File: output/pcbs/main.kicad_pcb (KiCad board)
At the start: 2 copper layers, 125.8 x 86.6 mm, 22 parts

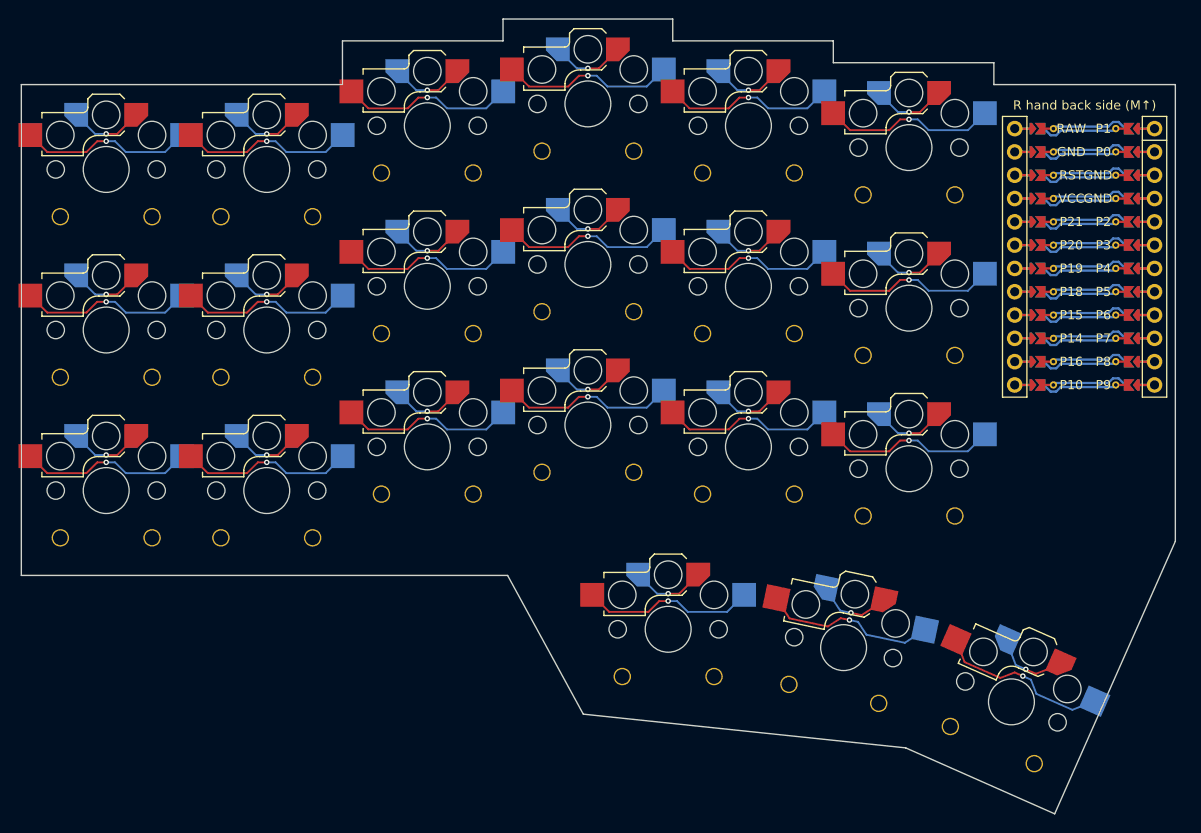
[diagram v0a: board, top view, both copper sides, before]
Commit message: feat: add more ref pos (9-14) and ref corners
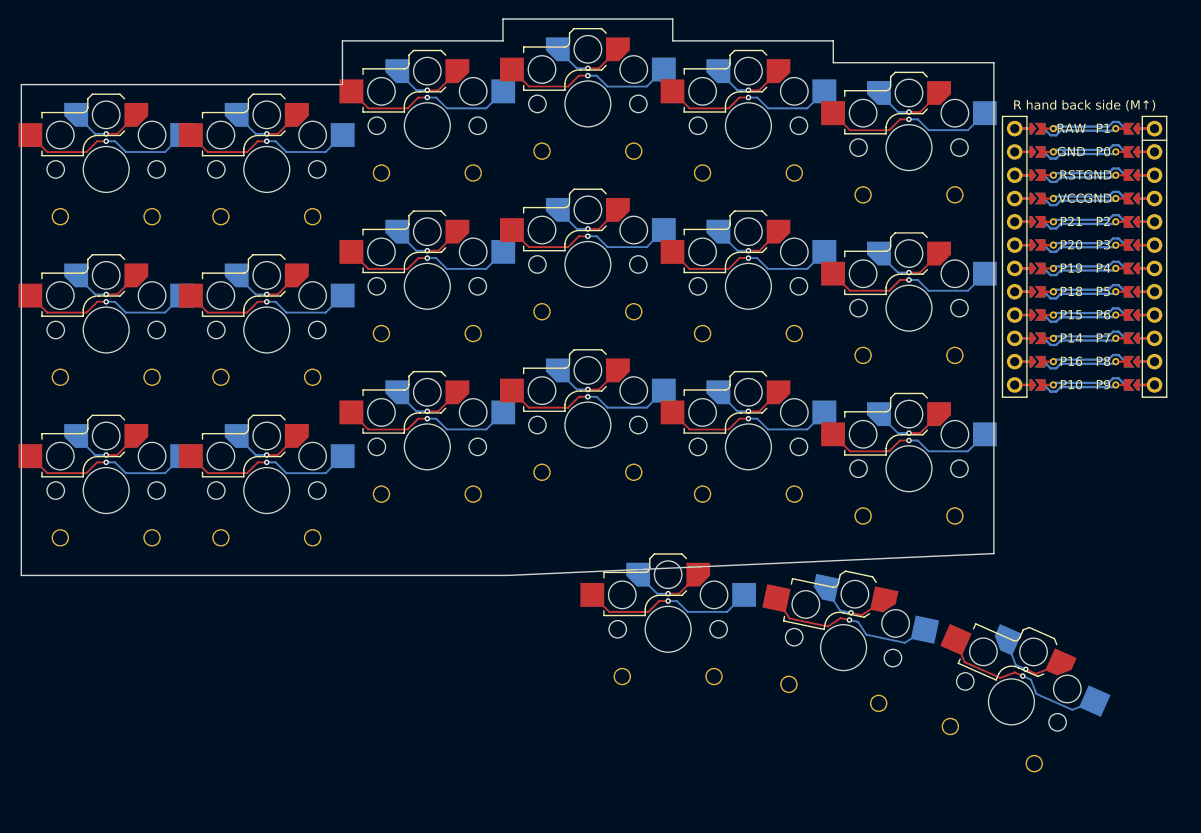
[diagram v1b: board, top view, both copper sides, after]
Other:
- board size 125.8 x 86.6 mm -> 106 x 60.6 mm

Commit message: refactor: minor refactor
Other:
- board size 106 x 60.6 mm -> 120.1 x 86.6 mm
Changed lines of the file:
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@@
   (title_block
     (title "main")
-    (date "2025-01-11")
+    (date "2025-01-12")
     (rev "v1.0.0")
     (company "Unknown")
@@
   (segment (start 110.340305 -12.235) (end 109.739695 -12.235) (width 0.25) (layer "B.Cu"))
   (segment (start 109.739695 -12.235) (end 109.234695 -11.73) (width 0.25) (layer "B.Cu"))
-  (gr_line (start 96.75 6.869) (end 96.75 -46.631) (layer Edge.Cuts) (stroke (width 0.15) (type default)))
-(gr_line (start -9.25 9.25) (end 43.75 9.25) (layer Edge.Cuts) (stroke (width 0.15) (type default)))
-(gr_line (start 25.75 -44.25) (end -9.25 -44.25) (layer Edge.Cuts) (stroke (width 0.15) (type default)))
-(gr_line (start -9.25 -44.25) (end -9.25 9.25) (layer Edge.Cuts) (stroke (width 0.15) (type default)))
+  (gr_line (start -9.25 9.25) (end 43.75 9.25) (layer Edge.Cuts) (stroke (width 0.15) (type default)))
+(gr_line (start -9.25 9.25) (end -9.25 -44.25) (layer Edge.Cuts) (stroke (width 0.15) (type default)))
+(gr_line (start -9.25 -44.25) (end 25.75 -44.25) (layer Edge.Cuts) (stroke (width 0.15) (type default)))
+(gr_line (start 25.75 -44.25) (end 25.75 -49.012) (layer Edge.Cuts) (stroke (width 0.15) (type default)))
 (gr_line (start 25.75 -49.012) (end 43.25 -49.012) (layer Edge.Cuts) (stroke (width 0.15) (type default)))
-(gr_line (start 25.75 -49.012) (end 25.75 -44.25) (layer Edge.Cuts) (stroke (width 0.15) (type default)))
-(gr_line (start 61.75 -49.012) (end 61.75 -51.393) (layer Edge.Cuts) (stroke (width 0.15) (type default)))
-(gr_line (start 61.75 -51.393) (end 43.25 -51.393) (layer Edge.Cuts) (stroke (width 0.15) (type default)))
-(gr_line (start 43.25 -51.393) (end 43.25 -49.012) (layer Edge.Cuts) (stroke (width 0.15) (type default)))
-(gr_line (start 79.25 -46.631) (end 79.25 -49.012) (layer Edge.Cuts) (stroke (width 0.15) (type default)))
+(gr_line (start 43.25 -49.012) (end 43.25 -51.393) (layer Edge.Cuts) (stroke (width 0.15) (type default)))
+(gr_line (start 43.25 -51.393) (end 61.75 -51.393) (layer Edge.Cuts) (stroke (width 0.15) (type default)))
+(gr_line (start 61.75 -51.393) (end 61.75 -49.012) (layer Edge.Cuts) (stroke (width 0.15) (type default)))
 (gr_line (start 61.75 -49.012) (end 79.25 -49.012) (layer Edge.Cuts) (stroke (width 0.15) (type default)))
+(gr_line (start 79.25 -49.012) (end 79.25 -46.631) (layer Edge.Cuts) (stroke (width 0.15) (type default)))
 (gr_line (start 79.25 -46.631) (end 96.75 -46.631) (layer Edge.Cuts) (stroke (width 0.15) (type default)))
-(gr_line (start 96.75 6.869) (end 43.75 9.25) (layer Edge.Cuts) (stroke (width 0.15) (type default)))
+(gr_line (start 96.75 -46.631) (end 96.75 6.869) (layer Edge.Cuts) (stroke (width 0.15) (type default)))
+(gr_line (start 43.75 9.25) (end 52 24.369) (layer Edge.Cuts) (stroke (width 0.15) (type default)))
+(gr_line (start 52 24.369) (end 87.1375839 28.0435087) (layer Edge.Cuts) (stroke (width 0.15) (type default)))
+(gr_line (start 87.1375839 28.0435087) (end 103.3780884 35.2335285) (layer Edge.Cuts) (stroke (width 0.15) (type default)))
+(gr_line (start 103.3780884 35.2335285) (end 110.8673033 18.317215) (layer Edge.Cuts) (stroke (width 0.15) (type default)))
+(gr_line (start 110.8673033 18.317215) (end 93.9509898 10.8280001) (layer Edge.Cuts) (stroke (width 0.15) (type default)))
+(gr_line (start 93.9509898 10.8280001) (end 96.75 6.869) (layer Edge.Cuts) (stroke (width 0.15) (type default)))
 )

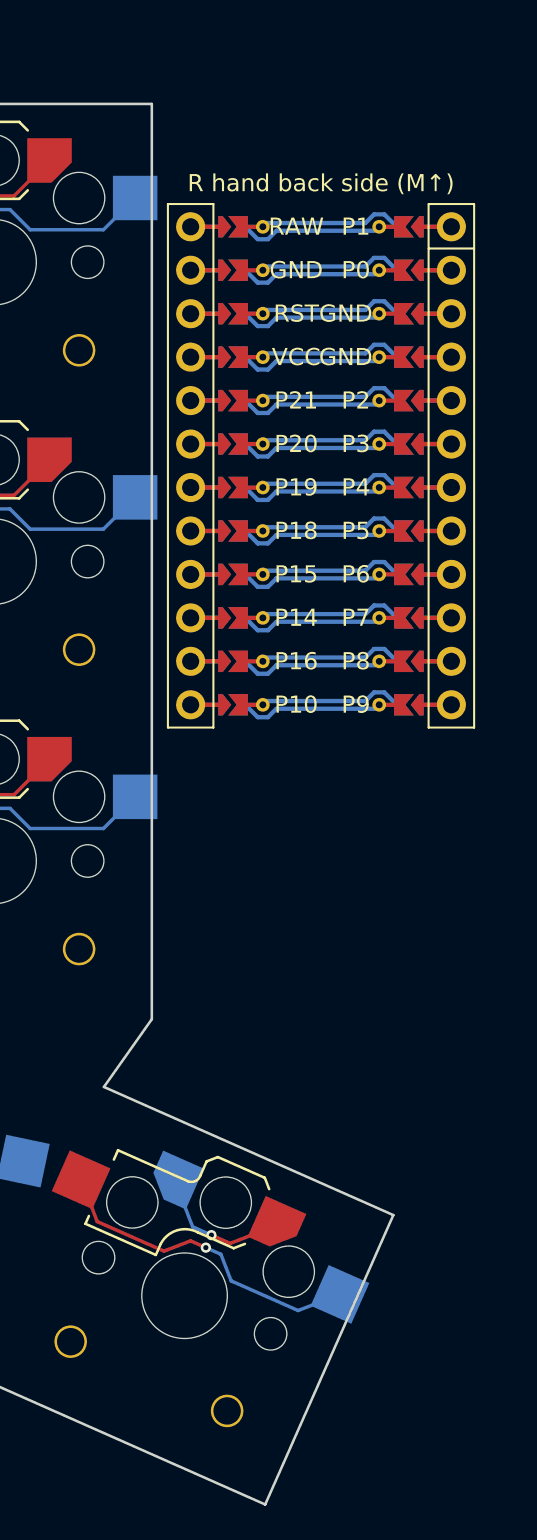
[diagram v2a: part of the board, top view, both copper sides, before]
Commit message: feat: update mcu plate calculations
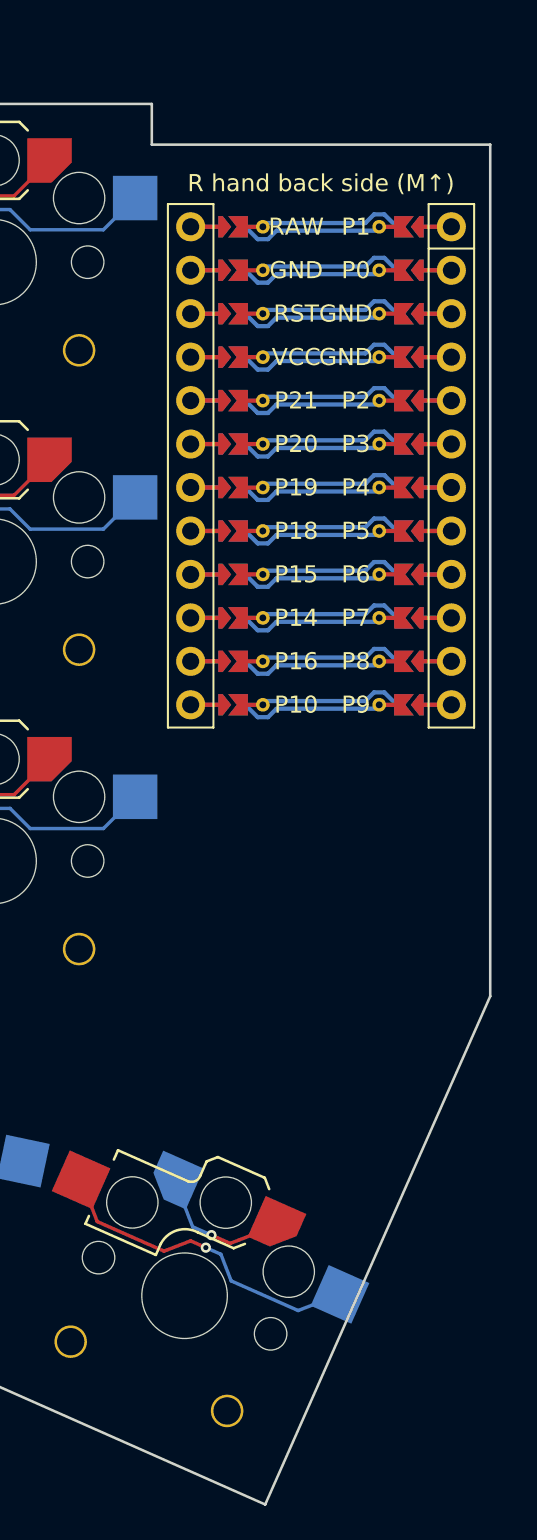
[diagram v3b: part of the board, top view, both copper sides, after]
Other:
- board size 120.1 x 86.6 mm -> 125.8 x 86.6 mm
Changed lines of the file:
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@@
   (segment (start 110.340305 -12.235) (end 109.739695 -12.235) (width 0.25) (layer "B.Cu"))
   (segment (start 109.739695 -12.235) (end 109.234695 -11.73) (width 0.25) (layer "B.Cu"))
-  (gr_line (start -9.25 9.25) (end 43.75 9.25) (layer Edge.Cuts) (stroke (width 0.15) (type default)))
+  (gr_line (start 96.75 -44.25) (end 116.53 -44.25) (layer Edge.Cuts) (stroke (width 0.15) (type default)))
+(gr_line (start 116.53 -44.25) (end 116.53 5.5265615) (layer Edge.Cuts) (stroke (width 0.15) (type default)))
+(gr_line (start 103.3780884 35.2335285) (end 116.53 5.5265615) (layer Edge.Cuts) (stroke (width 0.15) (type default)))
+(gr_line (start -9.25 9.25) (end 43.75 9.25) (layer Edge.Cuts) (stroke (width 0.15) (type default)))
 (gr_line (start -9.25 9.25) (end -9.25 -44.25) (layer Edge.Cuts) (stroke (width 0.15) (type default)))
 (gr_line (start -9.25 -44.25) (end 25.75 -44.25) (layer Edge.Cuts) (stroke (width 0.15) (type default)))
@@
 (gr_line (start 79.25 -49.012) (end 79.25 -46.631) (layer Edge.Cuts) (stroke (width 0.15) (type default)))
 (gr_line (start 79.25 -46.631) (end 96.75 -46.631) (layer Edge.Cuts) (stroke (width 0.15) (type default)))
-(gr_line (start 96.75 -46.631) (end 96.75 6.869) (layer Edge.Cuts) (stroke (width 0.15) (type default)))
+(gr_line (start 96.75 -46.631) (end 96.75 -44.25) (layer Edge.Cuts) (stroke (width 0.15) (type default)))
 (gr_line (start 43.75 9.25) (end 52 24.369) (layer Edge.Cuts) (stroke (width 0.15) (type default)))
 (gr_line (start 52 24.369) (end 87.1375839 28.0435087) (layer Edge.Cuts) (stroke (width 0.15) (type default)))
 (gr_line (start 87.1375839 28.0435087) (end 103.3780884 35.2335285) (layer Edge.Cuts) (stroke (width 0.15) (type default)))
-(gr_line (start 103.3780884 35.2335285) (end 110.8673033 18.317215) (layer Edge.Cuts) (stroke (width 0.15) (type default)))
-(gr_line (start 110.8673033 18.317215) (end 93.9509898 10.8280001) (layer Edge.Cuts) (stroke (width 0.15) (type default)))
-(gr_line (start 93.9509898 10.8280001) (end 96.75 6.869) (layer Edge.Cuts) (stroke (width 0.15) (type default)))
 )
